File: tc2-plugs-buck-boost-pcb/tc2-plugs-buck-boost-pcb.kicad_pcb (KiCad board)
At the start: 4 copper layers, 65 x 19.5 mm, 61 parts, among them J1 JCON_M16_04Pin, J2 JCON_M16_2+4Pin, J3 Conn_02x06_Odd_Even, Q1 Q_PMOS_GSD, Q2 Q_PMOS_GSD, Q3 AO3400A, U1 TPS63070RNMR, U2 TPS63071

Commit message: v0.4.0
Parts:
- removed R9: 33k, Resistor_SMD:R_0603_1608Metric
- added D2: UESD3.3DT5G, Package_TO_SOT_SMD:SOT-723, F.Cu at (15.3, -7.18)
- added D3: MMBZ9V1ALT1G, Package_TO_SOT_SMD:SOT-23, F.Cu at (15.5, -2.44)
- R10: value 22k -> 68k; footprint Resistor_SMD:R_0805_2012Metric -> Resistor_SMD:R_0402_1005Metric
- R7: value 560k -> 680k; footprint Resistor_SMD:R_1206_3216Metric -> Resistor_SMD:R_0805_2012Metric
- R8: value 150k -> 100k; footprint Resistor_SMD:R_0805_2012Metric -> Resistor_SMD:R_0402_1005Metric
- moved R10 3.34 mm to (-23.9, -8.67)
- moved R8 3.00 mm to (-22.0, -8.67), turned to 180 degrees
- moved R7 0.57 mm to (-28.1, -9.15)
- moved R4 0.07 mm to (-10.3, -14.4)
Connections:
- R7 pad 2: Net-(R7-Pad2) -> GND
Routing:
- net GND: track 7.08 -> 10.3 mm, vias 78 -> 82
- net BATT_SENSE_HV: track 23.7 -> 25.8 mm
- net Net-(R7-Pad2): track 1.47 -> 0.00 mm
- net Net-(R10-Pad1): track 1.73 -> 0.84 mm
- net SPEAKER_+: track 30.0 -> 30.5 mm
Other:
- board text added: "v0.4.0"
- board text removed: "V0.1.4"

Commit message: Small update for v0.4.1
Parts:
- R5, R6: footprint Resistor_SMD:R_1210_3225Metric -> Resistor_SMD:R_0805_2012Metric
- R7: footprint Resistor_SMD:R_0805_2012Metric -> Resistor_SMD:R_0603_1608Metric
- moved R7 0.83 mm to (-27.6, -8.52)
- moved R10 0.80 mm to (-24.4, -8.04)
- moved R8 0.80 mm to (-22.5, -8.04)
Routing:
- net BATT_SENSE_LV: track 35.1 -> 34.2 mm
- net BATT_SENSE_HV: track 25.8 -> 25.2 mm
- net /+Batt: track 9.77 -> 10.3 mm
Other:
- board text added: "${TAG}"
- board text removed: "v0.4.0"

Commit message: panelize WIP
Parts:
- added REF**: Tab, kikit:Tab, F.Cu at (7.00, 5.00)
- added REF**: Tab, kikit:Tab, F.Cu at (-20.0, -16.0)
- added REF**: Tab, kikit:Tab, F.Cu at (22.0, -15.0)
- added REF**: Tab, kikit:Tab, F.Cu at (27.0, 5.00)
- added REF**: Tab, kikit:Tab, F.Cu at (-13.0, 5.00)
- added REF**: Tab, kikit:Tab, F.Cu at (35.0, -5.00)
- added REF**: Tab, kikit:Tab, F.Cu at (-31.0, -6.00)

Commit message: Adding panel
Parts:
- removed D2: UESD3.3DT5G, Package_TO_SOT_SMD:SOT-723
- removed D3: MMBZ9V1ALT1G, Package_TO_SOT_SMD:SOT-23
- removed the REF** at (7.00, 5.00)
- removed the REF** at (-20.0, -16.0)
- removed the REF** at (22.0, -15.0)
- removed the REF** at (27.0, 5.00)
- removed the REF** at (-13.0, 5.00)
- removed the REF** at (35.0, -5.00)
- removed the REF** at (-31.0, -6.00)
- added D5: SMF05CT1G, cacophony-library:SOT-363_L2.0-W1.3-P0.65-LS2.1-BR, F.Cu at (15.2, -5.70)
- added R9: 100k, Resistor_SMD:R_0402_1005Metric, F.Cu at (-9.90, 2.70)
- added REF**: Tab_8mm, kikit:Tab_8mm, F.Cu at (7.00, 4.30)
- added REF**: Tab_8mm, kikit:Tab_8mm, F.Cu at (35.3, -5.00)
- added REF**: Tab_8mm, kikit:Tab_8mm, F.Cu at (-13.0, 4.30)
- added REF**: Tab_8mm, kikit:Tab_8mm, F.Cu at (22.0, -14.3)
- added REF**: Tab_8mm, kikit:Tab_8mm, F.Cu at (-20.0, -15.8)
- added REF**: Tab_8mm, kikit:Tab_8mm, F.Cu at (-30.3, -6.10)
- added REF**: Tab_8mm, kikit:Tab_8mm, F.Cu at (27.0, 4.30)
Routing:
- net +3V3: track 31.5 -> 48.5 mm, vias 0 -> 1
- net SPEAKER_-: track 32.9 -> 36.8 mm, vias 4 -> 5
- net SPEAKER_+: track 30.5 -> 31.9 mm
- net GND: track 10.5 -> 9.39 mm
- net OUT_TX: track 28.3 -> 29.1 mm
- net 5V_EN: track 25.7 -> 26.2 mm

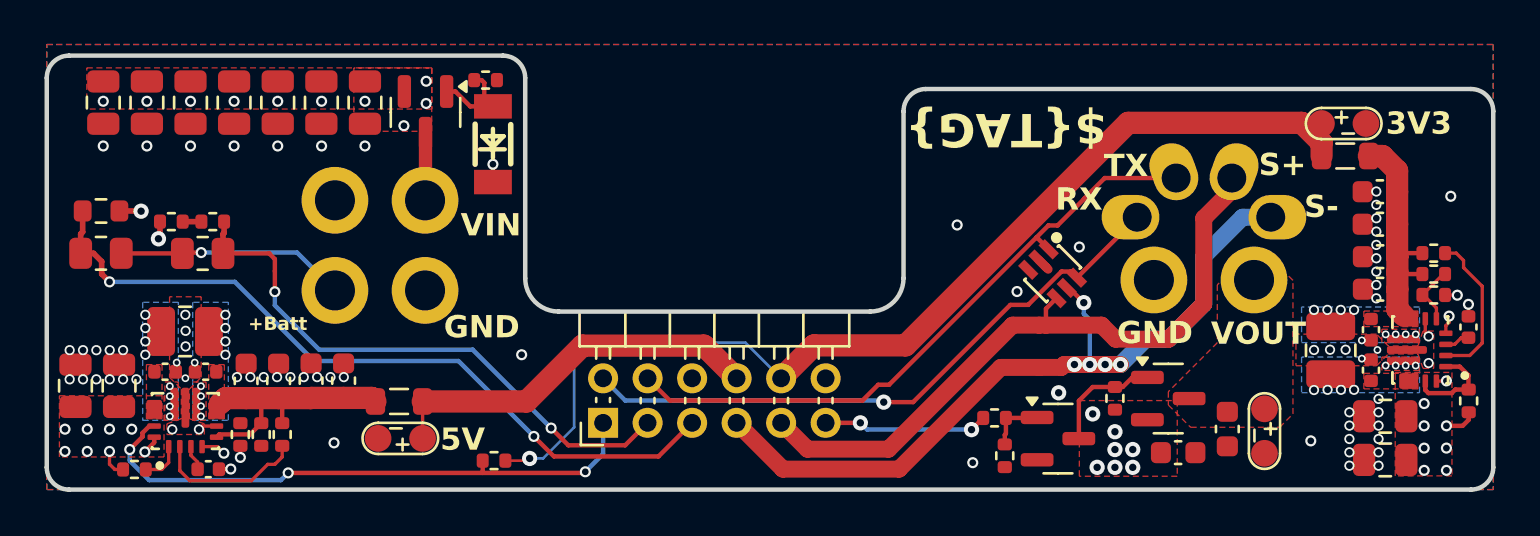
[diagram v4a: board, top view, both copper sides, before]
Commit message: Update to use touch sensor
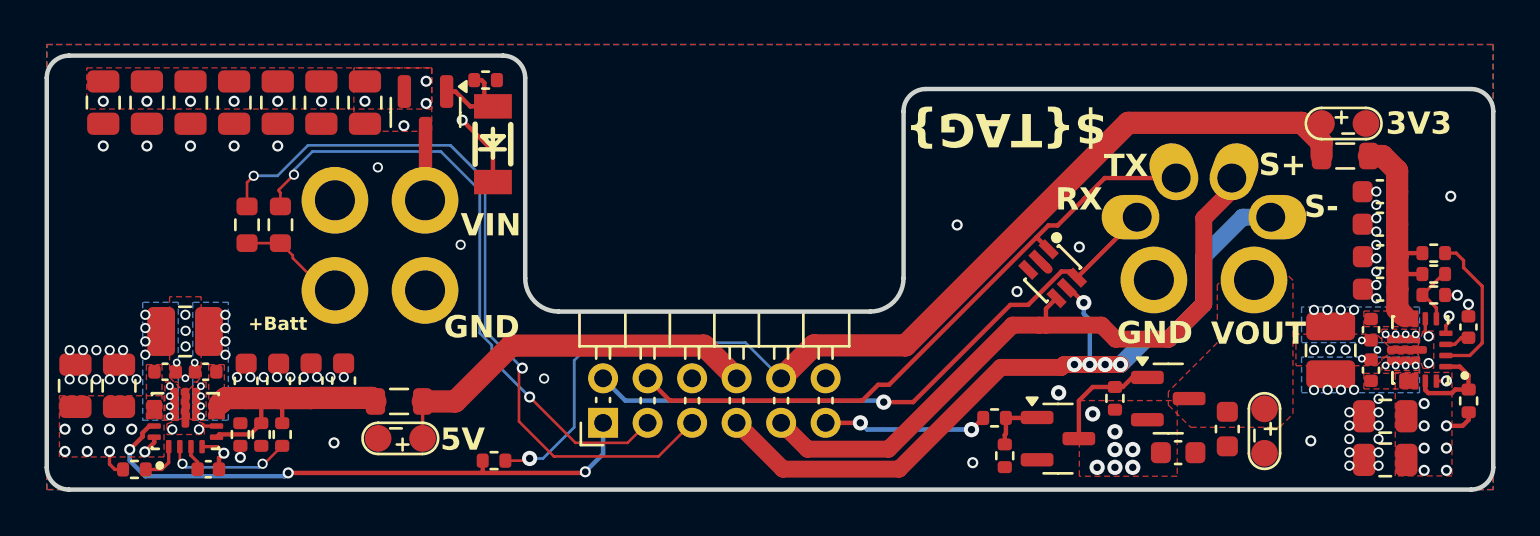
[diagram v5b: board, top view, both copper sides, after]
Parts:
- removed R10: 68k, Resistor_SMD:R_0402_1005Metric
- removed R5, R6: 2M, Resistor_SMD:R_0805_2012Metric
- removed R7: 680k, Resistor_SMD:R_0603_1608Metric
- removed R8: 100k, Resistor_SMD:R_0402_1005Metric
- removed the REF** at (7.00, 4.30)
- removed the REF** at (35.3, -5.00)
- removed the REF** at (-13.0, 4.30)
- removed the REF** at (22.0, -14.3)
- removed the REF** at (-20.0, -15.8)
- removed the REF** at (-30.3, -6.10)
- removed the REF** at (27.0, 4.30)
- added R202: 1M, Resistor_SMD:R_0603_1608Metric, F.Cu at (-19.5, -7.90)
- added R203: 1M, Resistor_SMD:R_0603_1608Metric, F.Cu at (-21.0, -7.90)
- added REF**: Tab8mm, cacophony-library:Tab8mm, F.Cu at (-30.3, -6.10)
- added REF**: Tab8mm, cacophony-library:Tab8mm, F.Cu at (35.3, -5.00)
- added REF**: Tab8mm, cacophony-library:Tab8mm, F.Cu at (27.0, 4.30)
- added REF**: Tab8mm, cacophony-library:Tab8mm, F.Cu at (7.00, 4.30)
- added REF**: Tab8mm, cacophony-library:Tab8mm, F.Cu at (22.0, -14.3)
- added REF**: Tab8mm, cacophony-library:Tab8mm, F.Cu at (-18.0, 4.30)
- added REF**: Tab8mm, cacophony-library:Tab8mm, F.Cu at (-20.0, -15.8)
- renumbered C22 to C201, C23 to C202, C24 to C203, C25 to C204, C26 to C205, C2 to C206, C27 to C207, C1 to C208, C3 to C209, C4 to C210, C5 to C211, C6 to C212, C7 to C213, C8 to C214, C9 to C215, C10 to C216, C11 to C217, C12 to C218, C13 to C219, C14 to C220, C15 to C221, C16 to C222, C17 to C223, C18 to C224, C19 to C225, C20 to C226, C21 to C227, D1 to D201, D5 to D202, FB1 to FB201, FB2 to FB202, J1 to J201, J2 to J202, J3 to J203, L1 to L201, L2 to L202, Q2 to Q201, Q1 to Q202, Q3 to Q203, R4 to R201, R1 to R204, R2 to R205, R3 to R206, R11 to R207, R12 to R208, R13 to R209, R14 to R210, R9 to R211, R15 to R212, R16 to R213, R17 to R214, R18 to R215, TP1 to TP201, TP2 to TP202, TP3 to TP203, U1 to U201, U2 to U202
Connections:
- J201 pad 4: /+Batt -> Net-(J201-Pad4)
- J203 pad 3: BATT_SENSE_HV -> BATTERY_LV
- J203 pad 5: BATT_SENSE_LV -> BATTERY_HV
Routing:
- net BATT_SENSE_LV: track 34.2 -> 0.00 mm, vias 2 -> 0
- net BATTERY_HV: track 0.00 -> 33.8 mm, vias 0 -> 2
- net BATTERY_LV: track 0.00 -> 28.1 mm, vias 0 -> 2
- net BATT_SENSE_HV: track 25.2 -> 0.00 mm, vias 2 -> 0
- net /+Batt: track 10.3 -> 0.00 mm, vias 1 -> 0
- net Net-(J201-Pad4): track 0.00 -> 4.16 mm
- net VCC: track 3.53 -> 6.08 mm
- net SPEAKER_+: track 31.9 -> 29.7 mm
- net GND: track 9.39 -> 7.97 mm, vias 82 -> 79
- net Net-(U202-PG): track 6.80 -> 5.77 mm, vias 0 -> 2
- net Net-(R10-Pad1): track 0.84 -> 0.00 mm
- net Net-(D201-A): track 4.15 -> 3.60 mm
- added copper zone on In2.Cu, net GND

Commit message: Small updates
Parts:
- added C228: 1uF, Capacitor_SMD:C_1206_3216Metric, F.Cu at (-24.2, -7.80)
- added R217: 180R, Resistor_SMD:R_0402_1005Metric, F.Cu at (-19.4, -6.40)
- moved R202 1.20 mm to (-20.7, -7.80)
- moved R203 1.20 mm to (-22.2, -7.80)
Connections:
- R202 pad 1: Net-(J201-Pad4) -> Net-(C228-Pad1)
- R203 pad 1: Net-(J201-Pad4) -> Net-(C228-Pad1)
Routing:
- net Net-(C228-Pad1): track 0.00 -> 5.10 mm
- net Net-(J201-Pad4): track 4.16 -> 2.74 mm
- net BATTERY_LV: track 28.1 -> 28.8 mm
- net BATTERY_HV: track 33.8 -> 34.4 mm

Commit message: Change to through hole connector and add simcard PCB to pannel
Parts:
- moved REF** 8.00 mm to (19.0, 4.30)
- moved REF** 8.00 mm to (-1.00, 4.30)
- moved REF** 6.83 mm to (15.2, -14.3)
- moved REF** 2.29 mm to (-17.7, -15.8)
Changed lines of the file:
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@@
 	(footprint "cacophony-library:Tab8mm"
 		(layer "F.Cu")
-		(at 27 4.3 90)
+		(at 19 4.3 90)
 		(descr "A symbol representing annotation for tab placement")
 		(property "Reference" "REF**"
@@
 	(footprint "cacophony-library:Tab8mm"
 		(layer "F.Cu")
-		(at 7 4.3 90)
+		(at -1 4.3 90)
 		(descr "A symbol representing annotation for tab placement")
 		(property "Reference" "REF**"
@@
 	(footprint "cacophony-library:Tab8mm"
 		(layer "F.Cu")
-		(at 22 -14.3 -90)
+		(at 15.17 -14.3 -90)
 		(descr "A symbol representing annotation for tab placement")
 		(property "Reference" "REF**"
-			(at -0.25 -2 -90)
+			(at -0.25 -2 90)
 			(layer "F.SilkS")
 			(hide yes)
@@
 		)
 		(property "Value" "Tab8mm"
-			(at -3 -1 -90)
+			(at -3 -1 90)
 			(layer "Dwgs.User")
 			(effects
@@
 	(footprint "cacophony-library:Tab8mm"
 		(layer "F.Cu")
-		(at -20 -15.8 -90)
+		(at -17.711 -15.8 -90)
 		(descr "A symbol representing annotation for tab placement")
 		(property "Reference" "REF**"
-			(at -0.25 -2 -90)
+			(at -0.25 -2 90)
 			(layer "F.SilkS")
 			(hide yes)
@@
 		)
 		(property "Value" "Tab8mm"
-			(at -3 -1 -90)
+			(at -3 -1 90)
 			(layer "Dwgs.User")
 			(effects

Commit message: Version v0.7.0
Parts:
- moved TP202 17.2 mm to (11.3, -9.38)
- moved C217 3.30 mm to (32.9, -7.93), turned to 0 degrees
- moved TP203 2.81 mm to (-16.9, 2.00)
- moved FB201 2.39 mm to (30.7, -10.4), turned to 90 degrees
- moved C228 0.67 mm to (-24.1, -8.46)
- moved REF** 0.30 mm to (-17.7, -15.5)
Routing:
- net +3V3: track 48.5 -> 17.0 mm, vias 1 -> 10
- net +5V: track 17.4 -> 0.00 mm, vias 0 -> 9
- net /3V3_PHY: track 10.3 -> 9.20 mm
- net Net-(C228-Pad1): track 5.10 -> 4.18 mm
- net GND: vias 79 -> 76
- net /5V_L2: vias 8 -> 7
- net /5V_L1: vias 8 -> 7
- net /3V3_L2: vias 8 -> 7
- net /3V3_L1: vias 8 -> 7
- added copper zone on F.Cu, net +3V3
- added copper zone on In3.Cu, net +3V3
- added copper zone on F.Cu, net +5V
- added copper zone on In3.Cu, net +5V
- added copper zone on In4.Cu, net GND
- removed copper zone on In2.Cu, net GND
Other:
- copper layers 4 -> 6
